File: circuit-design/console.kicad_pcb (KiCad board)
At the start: 2 copper layers, 80 x 50.5 mm, 13 parts, among them J1 CARTRIDGE, J2 POWER, J3 VIDEO (YELLOW), J4 AUDIO (WHITE), J5 PAD 0, J6 PAD 1, J7 PAD 2, J8 PAD 3, SW1 POWER_SW, SW2 RESET_SW

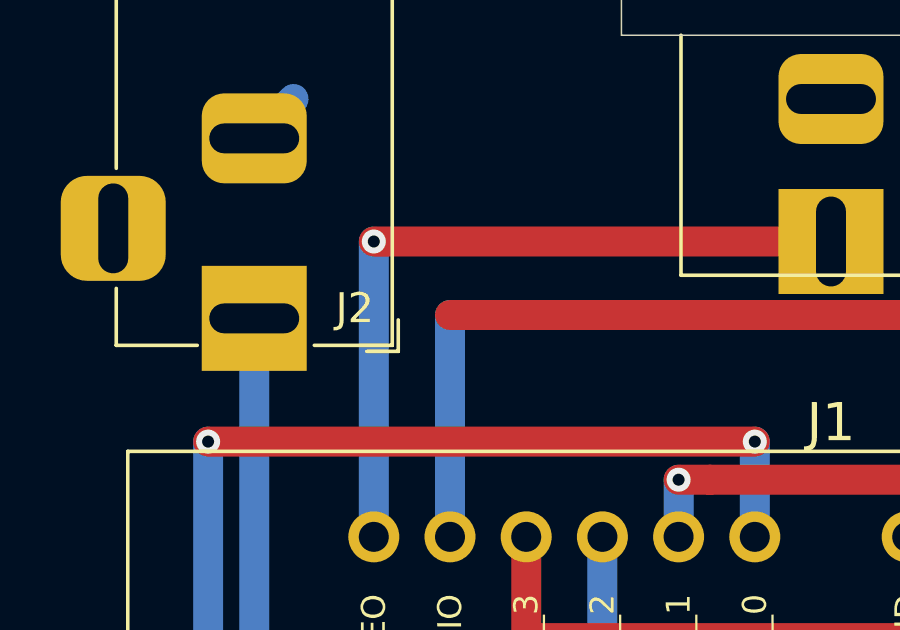
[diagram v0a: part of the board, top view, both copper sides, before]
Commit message: Add missing audio via.
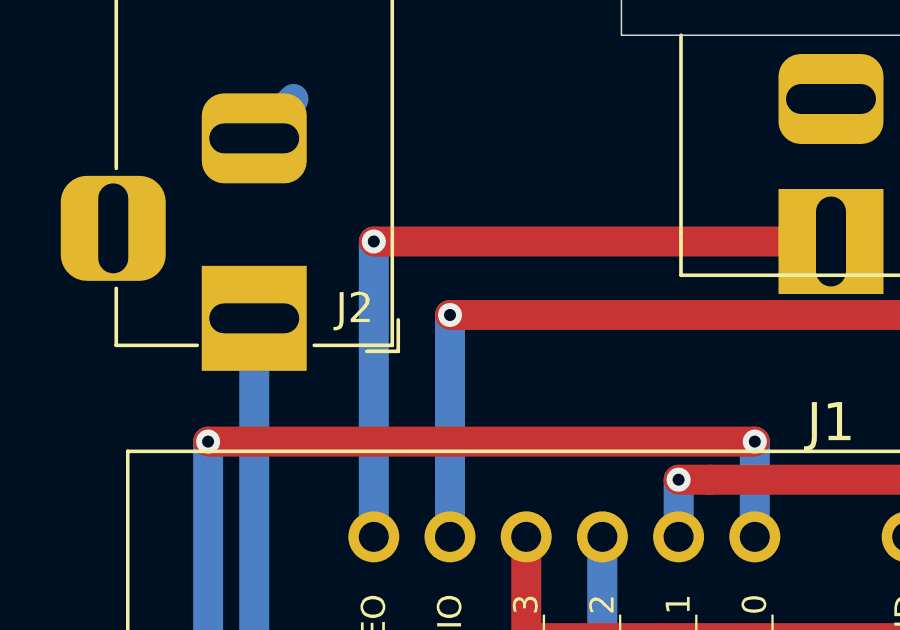
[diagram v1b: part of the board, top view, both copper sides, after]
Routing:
- net AUDIO: vias 0 -> 1

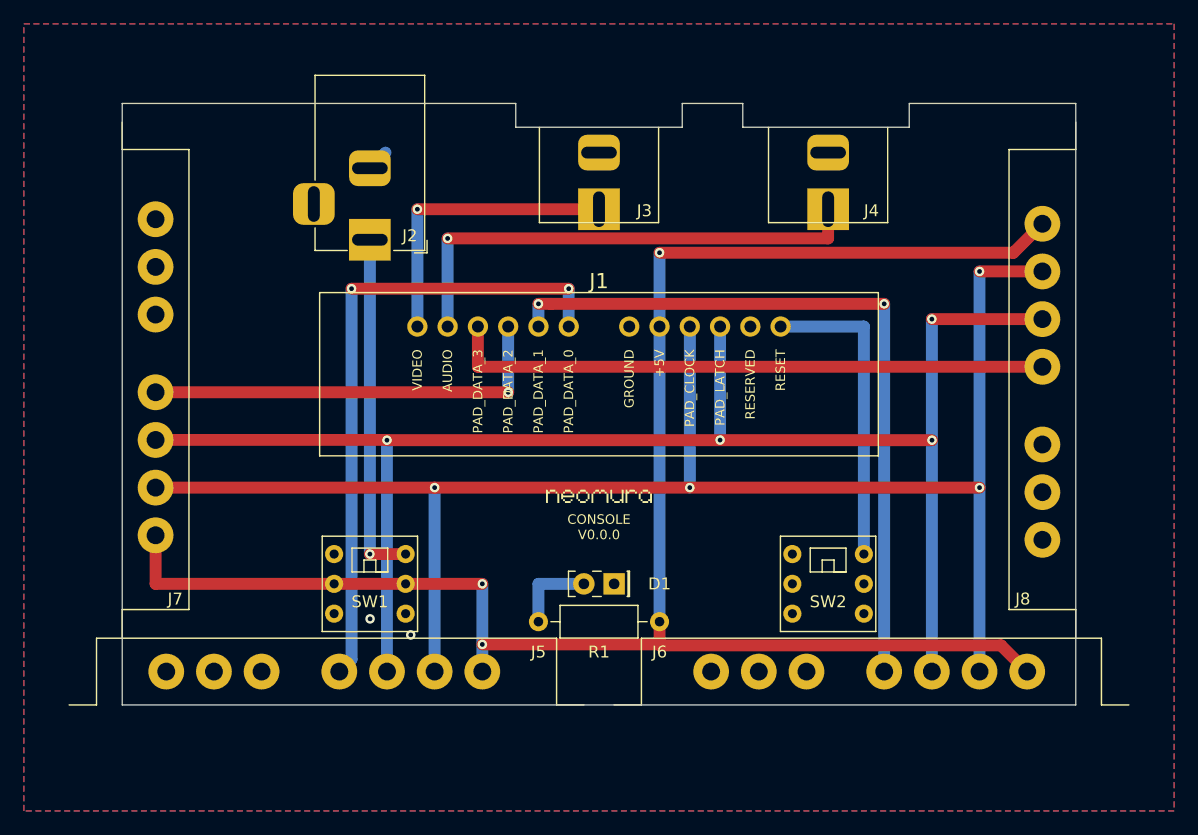
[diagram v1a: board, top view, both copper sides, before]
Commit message: Fix alignment of DC jack and remove need for slots on back edge.
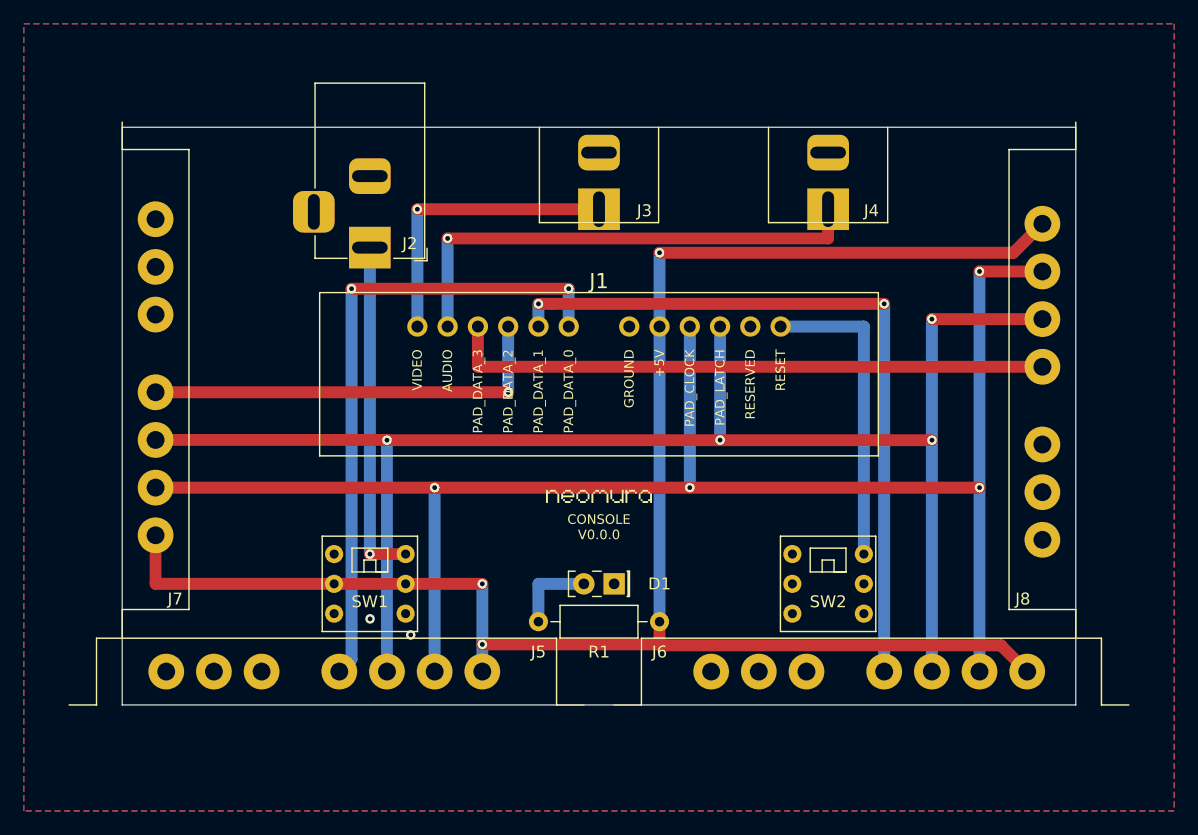
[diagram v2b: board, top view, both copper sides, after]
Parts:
- moved J2 0.66 mm to (163.7, 49.3)
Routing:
- net GND: track 1.86 -> 0.00 mm
- net Net-(J2-Pad1): track 29.4 -> 28.7 mm
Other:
- board size 80 x 50.5 mm -> 80 x 48.5 mm

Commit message: Redesign to support new cartridge connector.
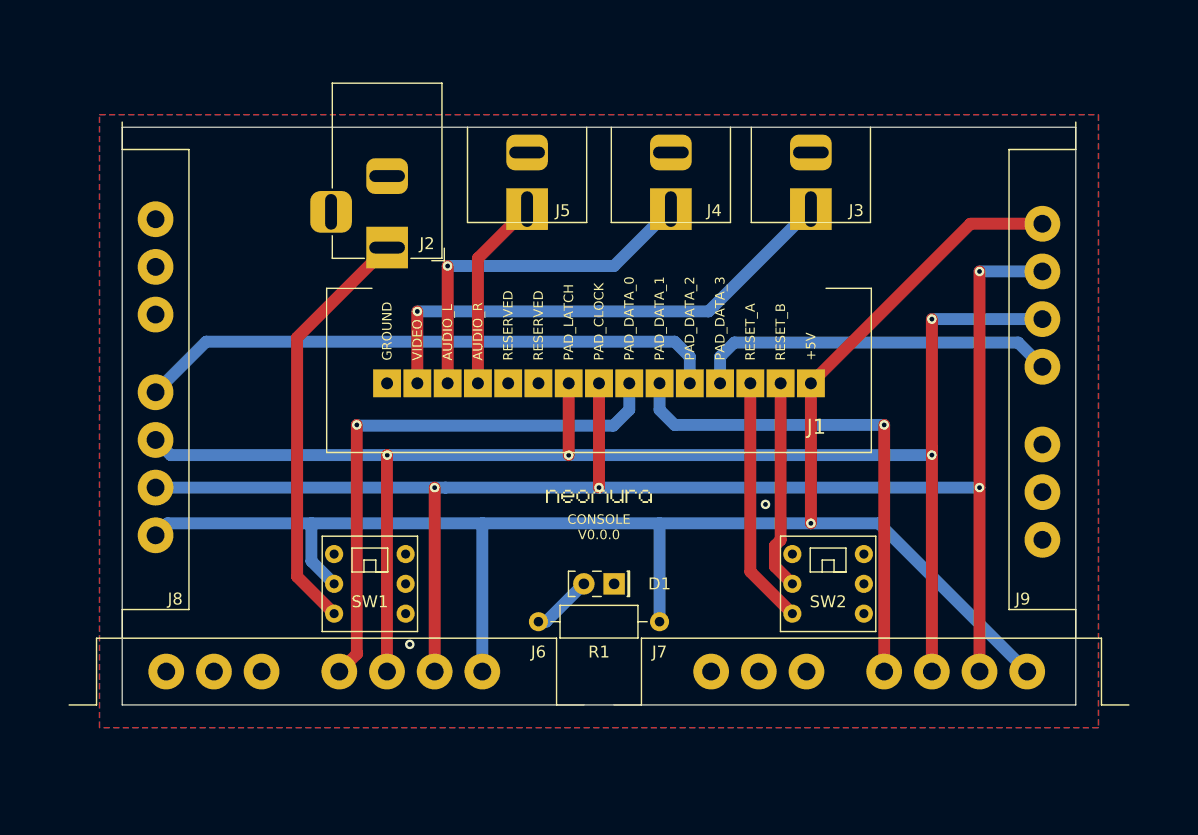
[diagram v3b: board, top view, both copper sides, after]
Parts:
- added J5: AUDIO (RED), Neomura_Console:RCA_Jack, F.Cu at (176.8, 37.1)
- moved J3 17.8 mm to (200.7, 37.1)
- moved J4 13.2 mm to (188.9, 37.1)
- moved J1 4.76 mm to (182.9, 60.6)
- moved J2 1.44 mm to (165.1, 49.3)
- renumbered J5 to J6, J6 to J7, J7 to J8, J8 to J9
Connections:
- J1 pad 1: VIDEO -> GND
- J1 pad 10: PAD_LATCH -> PAD_DATA_1
- J1 pad 11: Net-(J1-Pad11) -> PAD_DATA_2
- J1 pad 12: RESET -> PAD_DATA_3
- J1 pad 2: AUDIO -> VIDEO
- J1 pad 3: PAD_DATA_3 -> AUDIO_L
- J1 pad 4: PAD_DATA_2 -> AUDIO_R
- J1 pad 5: PAD_DATA_1 -> Net-(J1-Pad5)
- J1 pad 6: PAD_DATA_0 -> Net-(J1-Pad6)
- J1 pad 7: GND -> PAD_LATCH
- J1 pad 8: +5V -> PAD_CLOCK
- J1 pad 9: PAD_CLOCK -> PAD_DATA_0
- J4 pad 1: AUDIO -> AUDIO_L
- SW1 pad 2: Net-(J2-Pad1) -> Net-(SW1-Pad2)
- SW1 pad 3: +5V -> Net-(SW1-Pad3)
- SW1 pad 5: Net-(SW1-Pad5) -> Net-(J2-Pad1)
- SW2 pad 2: RESET -> Net-(SW2-Pad2)
- SW2 pad 3: GND -> Net-(SW2-Pad3)
- SW2 pad 5: Net-(SW2-Pad5) -> RESET_A
- SW2 pad 6: GND -> RESET_B
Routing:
- net AUDIO: track 41.8 -> 0.00 mm, vias 1 -> 0
- net AUDIO_L: track 0.00 -> 30.6 mm, vias 0 -> 1
- net RESET: track 26.1 -> 0.00 mm
- net RESET_A: track 0.00 -> 20.8 mm
- net PAD_DATA_3: track 50.7 -> 30.6 mm
- net PAD_DATA_1: track 61.8 -> 42.3 mm, vias 2 -> 1
- net RESET_B: track 0.00 -> 17.6 mm
- net VIDEO: track 25.1 -> 42.6 mm
- net AUDIO_R: track 0.00 -> 16.3 mm
- net PAD_DATA_2: track 35.1 -> 49.3 mm, vias 1 -> 0
- net +5V: track 151.5 -> 142.0 mm, vias 3 -> 1
- net PAD_DATA_0: track 53.9 -> 47.0 mm, vias 2 -> 1
- net Net-(J2-Pad1): track 28.7 -> 35.1 mm, vias 1 -> 0
- net PAD_LATCH: track 132.9 -> 128.7 mm
- net PAD_CLOCK: track 136.9 -> 133.0 mm
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
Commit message: Remove unnecessary via.
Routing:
- net PAD_CLOCK: track 133.0 -> 129.9 mm, vias 4 -> 3
